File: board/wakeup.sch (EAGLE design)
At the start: 23 parts, among them IC2 ATMEGA48/88/168-AU, K1 PIN20X2, U1 EEPROM24

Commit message: Added pin header for tm1637 7-Segment display
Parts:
- added SL3: (no value), con-amp-quick:M04
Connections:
- net +5V: now also SL3.1
- net GND: now also SL3.4
- net MISO_SPI: now also SL3.2
- net SCLK_SPI: now also SL3.3
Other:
- note added: "CREE HiPower LED"
- note added: "Connector for TM1637 7-Segment Display"
- note added: "External Power Connector 5V"
- note added: "RaspberryPI GPIO Header"
- moved on the sheet: J1
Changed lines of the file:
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@@
 <part name="GND16" library="supply1" deviceset="GND" device=""/>
 <part name="P+3" library="supply1" deviceset="+5V" device=""/>
+<part name="SL3" library="con-amp-quick" deviceset="M04" device=""/>
+<part name="P+5" library="supply1" deviceset="+5V" device=""/>
+<part name="GND17" library="supply1" deviceset="GND" device=""/>
 </parts>
 <sheets>
@@
 <text x="289.56" y="16.51" size="1.778" layer="94" ratio="15">Checked  by:</text>
 <text x="374.65" y="5.08" size="2.54" layer="94" ratio="10">v0.1</text>
+<text x="127" y="165.1" size="1.778" layer="91">Connector for TM1637 7-Segment Display</text>
+<text x="40.64" y="111.76" size="1.778" layer="91">RaspberryPI GPIO Header</text>
+<text x="276.86" y="193.04" size="1.778" layer="91">CREE HiPower LED</text>
+<text x="198.12" y="231.14" size="1.778" layer="91">External Power Connector 5V</text>
 </plain>
 <instances>
@@
 <instance part="P+4" gate="VCC" x="134.62" y="127"/>
 <instance part="GND15" gate="1" x="134.62" y="78.74"/>
-<instance part="J1" gate="G$1" x="248.92" y="236.22"/>
+<instance part="J1" gate="G$1" x="205.74" y="238.76"/>
 <instance part="CREE_LED1" gate="G$1" x="320.04" y="238.76" rot="R90"/>
 <instance part="CREE_LED1" gate="G$2" x="320.04" y="200.66" rot="R90"/>
@@
 <attribute name="VALUE" x="203.2" y="210.82" size="1.778" layer="96" rot="R180"/>
 </instance>
+<instance part="SL3" gate="G$1" x="157.48" y="180.34" rot="R180"/>
+<instance part="P+5" gate="1" x="139.7" y="187.96" smashed="yes">
+<attribute name="VALUE" x="142.24" y="190.5" size="1.778" layer="96" rot="R180"/>
+</instance>
+<instance part="GND17" gate="1" x="139.7" y="172.72"/>
 </instances>
 <busses>
@@
 <pinref part="J1" gate="G$1" pin="2"/>
 <pinref part="J1" gate="G$1" pin="1"/>
-<wire x1="259.08" y1="236.22" x2="254" y2="236.22" width="0.1524" layer="91"/>
-<wire x1="254" y1="236.22" x2="254" y2="233.68" width="0.1524" layer="91"/>
-<label x="259.08" y="236.22" size="1.778" layer="95"/>
-<junction x="259.08" y="236.22"/>
-<junction x="254" y="236.22"/>
+<wire x1="215.9" y1="238.76" x2="210.82" y2="238.76" width="0.1524" layer="91"/>
+<wire x1="210.82" y1="238.76" x2="210.82" y2="236.22" width="0.1524" layer="91"/>
+<label x="215.9" y="238.76" size="1.778" layer="95"/>
+<junction x="215.9" y="238.76"/>
+<junction x="210.82" y="238.76"/>
 </segment>
 <segment>
@@
 <junction x="342.9" y="213.36"/>
 </segment>
+<segment>
+<pinref part="SL3" gate="G$1" pin="4"/>
+<wire x1="152.4" y1="175.26" x2="139.7" y2="175.26" width="0.1524" layer="91"/>
+<pinref part="GND17" gate="1" pin="GND"/>
+</segment>
 </net>
 <net name="+3V3" class="0">
@@
 <segment>
 <pinref part="J1" gate="G$1" pin="3"/>
-<wire x1="254" y1="238.76" x2="264.16" y2="238.76" width="0.1524" layer="91"/>
-<label x="264.16" y="238.76" size="1.778" layer="95"/>
-<junction x="264.16" y="238.76"/>
+<wire x1="210.82" y1="241.3" x2="220.98" y2="241.3" width="0.1524" layer="91"/>
+<label x="220.98" y="241.3" size="1.778" layer="95"/>
+<junction x="220.98" y="241.3"/>
+</segment>
+<segment>
+<pinref part="SL3" gate="G$1" pin="1"/>
+<wire x1="152.4" y1="182.88" x2="139.7" y2="182.88" width="0.1524" layer="91"/>
+<wire x1="139.7" y1="182.88" x2="139.7" y2="185.42" width="0.1524" layer="91"/>
+<pinref part="P+5" gate="1" pin="+5V"/>
 </segment>
 </net>
@@
 <label x="12.7" y="149.86" size="1.778" layer="95"/>
 </segment>
+<segment>
+<pinref part="SL3" gate="G$1" pin="2"/>
+<wire x1="152.4" y1="180.34" x2="139.7" y2="180.34" width="0.1524" layer="91"/>
+<label x="127" y="180.34" size="1.778" layer="95"/>
+</segment>
 </net>
 <net name="SCLK_SPI" class="0">
@@
 <label x="12.7" y="147.32" size="1.778" layer="95"/>
 </segment>
-</net>
+<segment>
+<pinref part="SL3" gate="G$1" pin="3"/>
+<wire x1="152.4" y1="177.8" x2="139.7" y2="177.8" width="0.1524" layer="91"/>
+<label x="127" y="177.8" size="1.778" layer="95"/>
+</segment>
+</net>

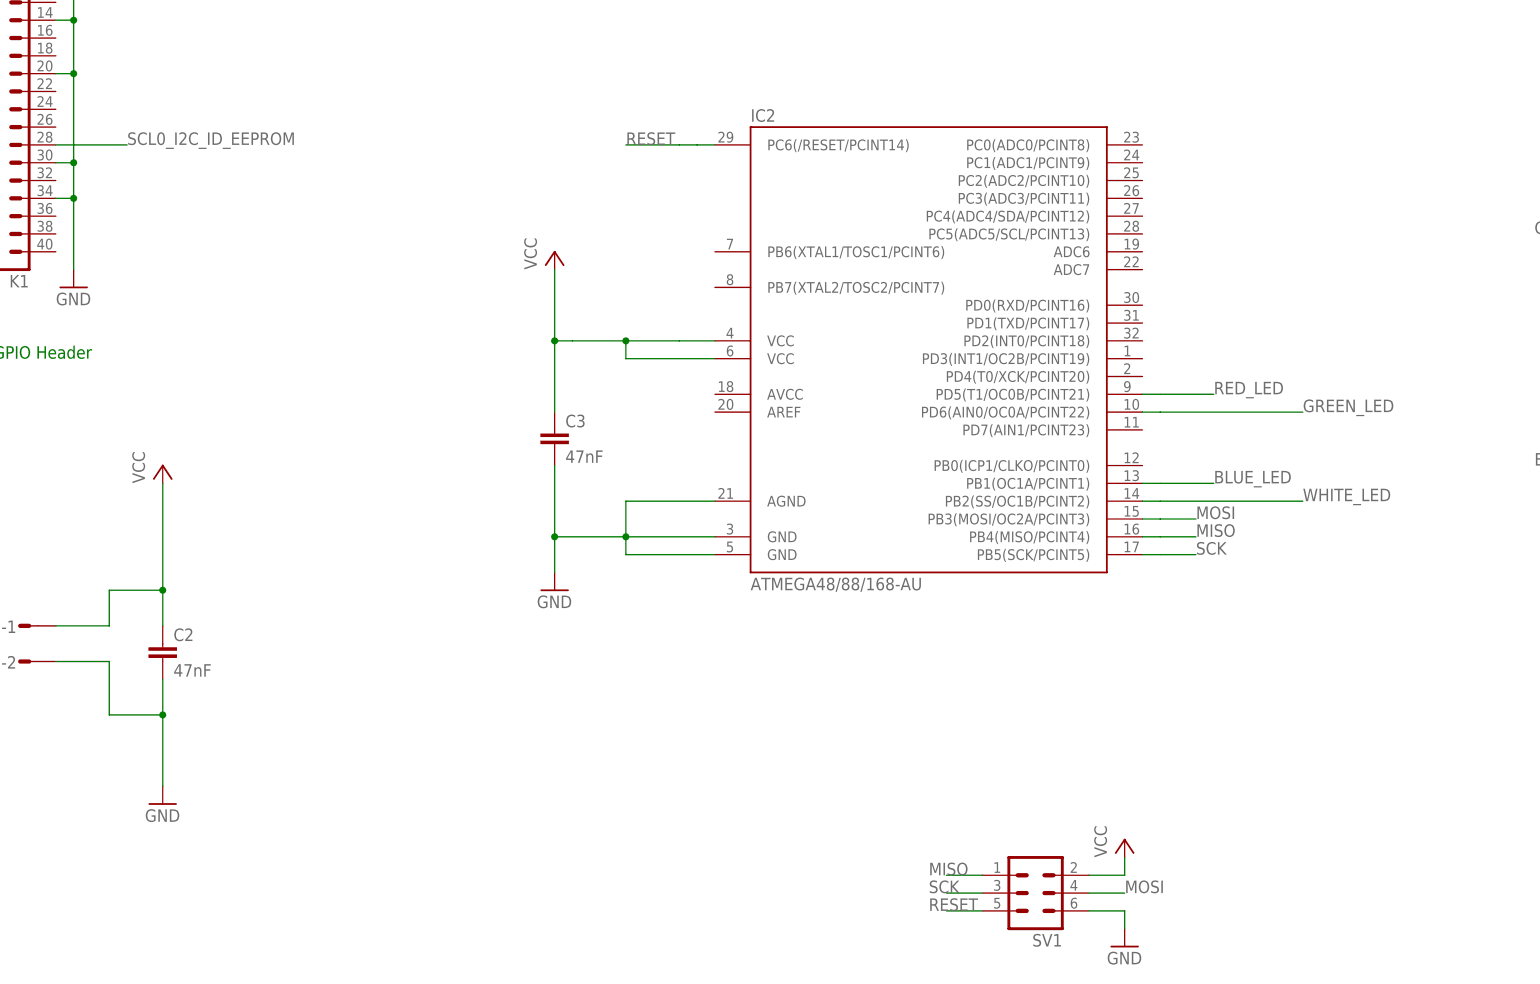
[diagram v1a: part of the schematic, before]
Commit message: Fixed FCC net, added I2C nets
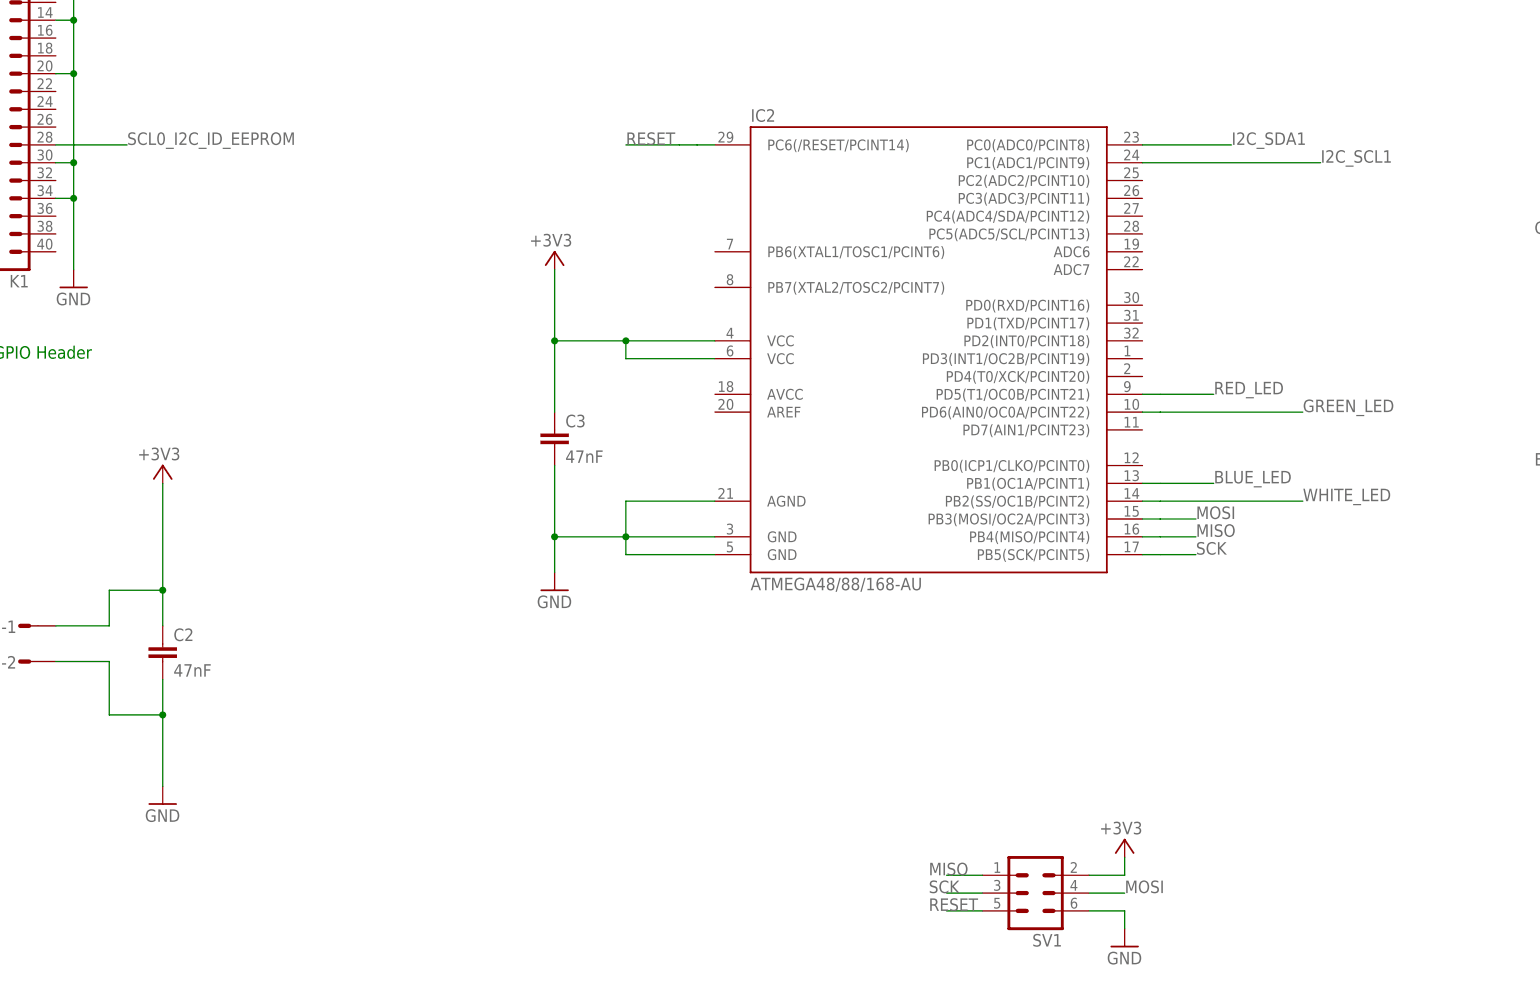
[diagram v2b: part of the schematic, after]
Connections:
- removed net VCC: C2.1, C3.1, IC2.VCC@1, IC2.VCC@2, SL2-1.S, SV1.2
- net +3V3: now also C2.1, C3.1, IC2.VCC@1, IC2.VCC@2, SL2-1.S, SV1.2
- net I2C_SCL1: now also IC2.PC1(ADC1/PCINT9)
- net I2C_SDA1: now also IC2.PC0(ADC0/PCINT8)
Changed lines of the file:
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@@
 <part name="P+1" library="supply1" deviceset="+5V" device=""/>
 <part name="SV1" library="con-ml" deviceset="ML6" device=""/>
-<part name="P+2" library="supply1" deviceset="VCC" device=""/>
 <part name="SL1" library="con-amp-quick" deviceset="M08" device=""/>
 <part name="GND6" library="supply1" deviceset="GND" device=""/>
 <part name="SL2" library="con-amp-quick" deviceset="M02S" device=""/>
 <part name="C2" library="rcl" deviceset="C-EU" device="C0805" value="47nF"/>
-<part name="P+7" library="supply1" deviceset="VCC" device=""/>
 <part name="GND7" library="supply1" deviceset="GND" device=""/>
 <part name="GND4" library="supply1" deviceset="GND" device=""/>
@@
 <part name="IC2" library="atmega8" deviceset="ATMEGA48/88/168" device="-AU"/>
 <part name="C3" library="rcl" deviceset="C-EU" device="C0805" value="47nF"/>
-<part name="P+4" library="supply1" deviceset="VCC" device=""/>
 <part name="GND15" library="supply1" deviceset="GND" device=""/>
 <part name="J1" library="con-jack" deviceset="JACK-PLUG" device="1"/>
@@
 <part name="P+5" library="supply1" deviceset="+5V" device=""/>
 <part name="GND17" library="supply1" deviceset="GND" device=""/>
+<part name="+3V2" library="supply1" deviceset="+3V3" device=""/>
+<part name="+3V3" library="supply1" deviceset="+3V3" device=""/>
+<part name="+3V6" library="supply1" deviceset="+3V3" device=""/>
 </parts>
 <sheets>
@@
 </instance>
 <instance part="SV1" gate="1" x="203.2" y="35.56" rot="R180"/>
-<instance part="P+2" gate="VCC" x="215.9" y="43.18"/>
 <instance part="SL1" gate="G$1" x="236.22" y="193.04" rot="R180"/>
 <instance part="GND6" gate="1" x="215.9" y="27.94"/>
@@
 <instance part="SL2" gate="-2" x="58.42" y="68.58"/>
 <instance part="C2" gate="G$1" x="78.74" y="71.12"/>
-<instance part="P+7" gate="VCC" x="78.74" y="96.52"/>
 <instance part="GND7" gate="1" x="78.74" y="48.26"/>
 <instance part="GND4" gate="1" x="302.26" y="152.4"/>
@@
 <instance part="IC2" gate="1" x="187.96" y="114.3"/>
 <instance part="C3" gate="G$1" x="134.62" y="101.6"/>
-<instance part="P+4" gate="VCC" x="134.62" y="127"/>
 <instance part="GND15" gate="1" x="134.62" y="78.74"/>
 <instance part="J1" gate="G$1" x="205.74" y="238.76"/>
@@
 </instance>
 <instance part="GND17" gate="1" x="139.7" y="172.72"/>
+<instance part="+3V2" gate="G$1" x="134.62" y="127" smashed="yes">
+<attribute name="VALUE" x="137.16" y="129.54" size="1.778" layer="96" rot="R180"/>
+</instance>
+<instance part="+3V3" gate="G$1" x="78.74" y="96.52" smashed="yes">
+<attribute name="VALUE" x="81.28" y="99.06" size="1.778" layer="96" rot="R180"/>
+</instance>
+<instance part="+3V6" gate="G$1" x="215.9" y="43.18" smashed="yes">
+<attribute name="VALUE" x="218.44" y="45.72" size="1.778" layer="96" rot="R180"/>
+</instance>
 </instances>
 <busses>
@@
 <junction x="43.18" y="175.26"/>
 </segment>
+<segment>
+<wire x1="157.48" y1="114.3" x2="144.78" y2="114.3" width="0.1524" layer="91"/>
+<wire x1="144.78" y1="114.3" x2="134.62" y2="114.3" width="0.1524" layer="91"/>
+<wire x1="134.62" y1="114.3" x2="134.62" y2="124.46" width="0.1524" layer="91"/>
+<pinref part="C3" gate="G$1" pin="1"/>
+<wire x1="134.62" y1="104.14" x2="134.62" y2="114.3" width="0.1524" layer="91"/>
+<junction x="134.62" y="114.3"/>
+<pinref part="IC2" gate="1" pin="VCC@2"/>
+<wire x1="157.48" y1="111.76" x2="144.78" y2="111.76" width="0.1524" layer="91"/>
+<wire x1="144.78" y1="111.76" x2="144.78" y2="114.3" width="0.1524" layer="91"/>
+<junction x="144.78" y="114.3"/>
+<pinref part="IC2" gate="1" pin="VCC@1"/>
+<pinref part="+3V2" gate="G$1" pin="+3V3"/>
+</segment>
+<segment>
+<wire x1="78.74" y1="78.74" x2="78.74" y2="93.98" width="0.1524" layer="91"/>
+<pinref part="C2" gate="G$1" pin="1"/>
+<wire x1="78.74" y1="73.66" x2="78.74" y2="78.74" width="0.1524" layer="91"/>
+<pinref part="SL2" gate="-1" pin="S"/>
+<wire x1="63.5" y1="73.66" x2="71.12" y2="73.66" width="0.1524" layer="91"/>
+<wire x1="71.12" y1="73.66" x2="71.12" y2="78.74" width="0.1524" layer="91"/>
+<wire x1="71.12" y1="78.74" x2="78.74" y2="78.74" width="0.1524" layer="91"/>
+<junction x="78.74" y="78.74"/>
+<pinref part="+3V3" gate="G$1" pin="+3V3"/>
+</segment>
+<segment>
+<pinref part="SV1" gate="1" pin="2"/>
+<wire x1="210.82" y1="38.1" x2="215.9" y2="38.1" width="0.1524" layer="91"/>
+<wire x1="215.9" y1="38.1" x2="215.9" y2="40.64" width="0.1524" layer="91"/>
+<pinref part="+3V6" gate="G$1" pin="+3V3"/>
+</segment>
 </net>
 <net name="SDA0_I2C_ID_EEPROM" class="0">
@@
 </segment>
 </net>
-<net name="VCC" class="0">
-<segment>
-<pinref part="P+7" gate="VCC" pin="VCC"/>
-<wire x1="78.74" y1="78.74" x2="78.74" y2="93.98" width="0.1524" layer="91"/>
-<pinref part="C2" gate="G$1" pin="1"/>
-<wire x1="78.74" y1="73.66" x2="78.74" y2="78.74" width="0.1524" layer="91"/>
-<pinref part="SL2" gate="-1" pin="S"/>
-<wire x1="63.5" y1="73.66" x2="71.12" y2="73.66" width="0.1524" layer="91"/>
-<wire x1="71.12" y1="73.66" x2="71.12" y2="78.74" width="0.1524" layer="91"/>
-<wire x1="71.12" y1="78.74" x2="78.74" y2="78.74" width="0.1524" layer="91"/>
-<junction x="78.74" y="78.74"/>
-</segment>
-<segment>
-<pinref part="SV1" gate="1" pin="2"/>
-<pinref part="P+2" gate="VCC" pin="VCC"/>
-<wire x1="210.82" y1="38.1" x2="215.9" y2="38.1" width="0.1524" layer="91"/>
-<wire x1="215.9" y1="38.1" x2="215.9" y2="40.64" width="0.1524" layer="91"/>
-</segment>
-<segment>
-<pinref part="P+4" gate="VCC" pin="VCC"/>
-<wire x1="152.4" y1="114.3" x2="144.78" y2="114.3" width="0.1524" layer="91"/>
-<wire x1="144.78" y1="114.3" x2="137.16" y2="114.3" width="0.1524" layer="91"/>
-<wire x1="137.16" y1="114.3" x2="134.62" y2="114.3" width="0.1524" layer="91"/>
-<wire x1="134.62" y1="114.3" x2="134.62" y2="124.46" width="0.1524" layer="91"/>
-<pinref part="C3" gate="G$1" pin="1"/>
-<wire x1="134.62" y1="104.14" x2="134.62" y2="114.3" width="0.1524" layer="91"/>
-<junction x="134.62" y="114.3"/>
-<pinref part="IC2" gate="1" pin="VCC@2"/>
-<wire x1="157.48" y1="111.76" x2="144.78" y2="111.76" width="0.1524" layer="91"/>
-<wire x1="144.78" y1="111.76" x2="144.78" y2="114.3" width="0.1524" layer="91"/>
-<junction x="144.78" y="114.3"/>
-<pinref part="IC2" gate="1" pin="VCC@1"/>
-<wire x1="157.48" y1="114.3" x2="152.4" y2="114.3" width="0.1524" layer="91"/>
-</segment>
-</net>
 <net name="MOSI" class="0">
 <segment>
@@
 <label x="27.94" y="172.72" size="1.778" layer="95"/>
 </segment>
+<segment>
+<pinref part="IC2" gate="1" pin="PC0(ADC0/PCINT8)"/>
+<wire x1="218.44" y1="142.24" x2="231.14" y2="142.24" width="0.1524" layer="91"/>
+<label x="231.14" y="142.24" size="1.778" layer="95"/>
+</segment>
 </net>
 <net name="I2C_SCL1" class="0">
@@
 <label x="27.94" y="170.18" size="1.778" layer="95"/>
 </segment>
-</net>
+<segment>
+<pinref part="IC2" gate="1" pin="PC1(ADC1/PCINT9)"/>
+<wire x1="218.44" y1="139.7" x2="243.84" y2="139.7" width="0.1524" layer="91"/>
+<label x="243.84" y="139.7" size="1.778" layer="95"/>
+</segment>
+</net>

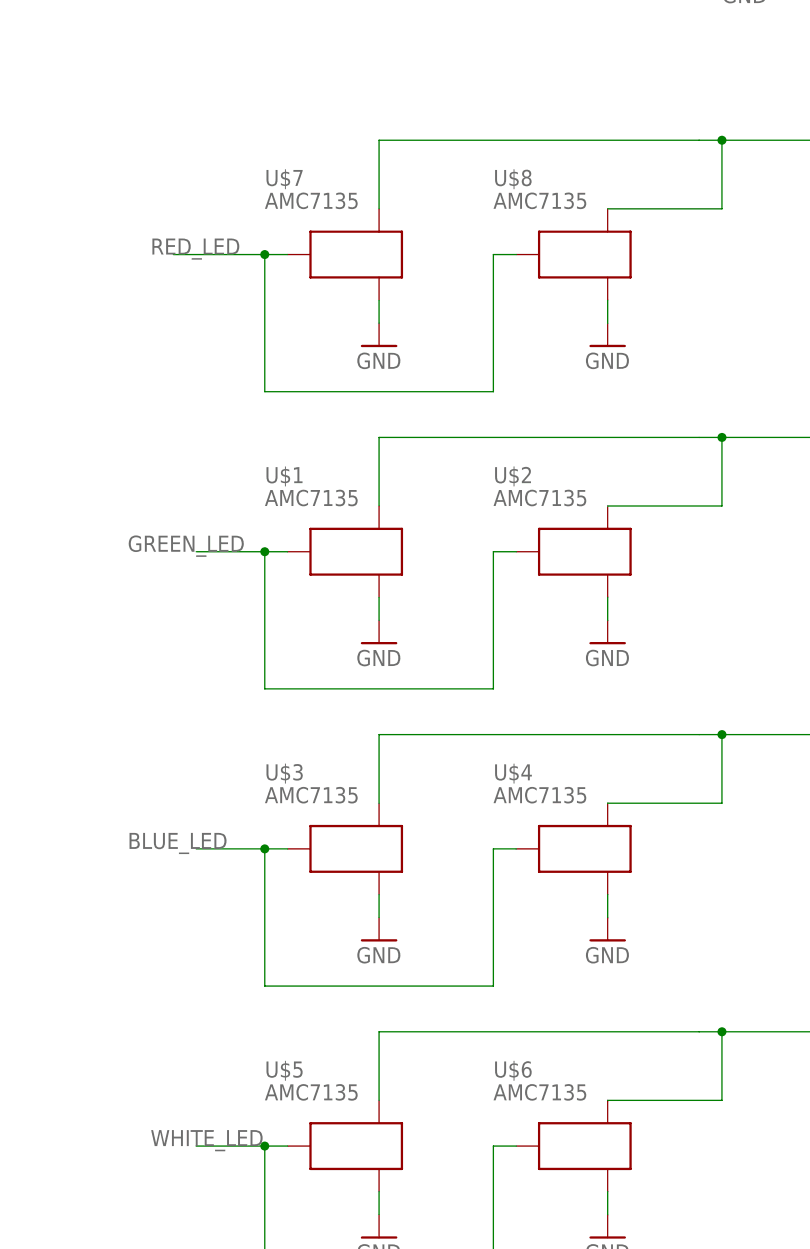
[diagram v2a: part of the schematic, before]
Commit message: Fixed some naming and added tag
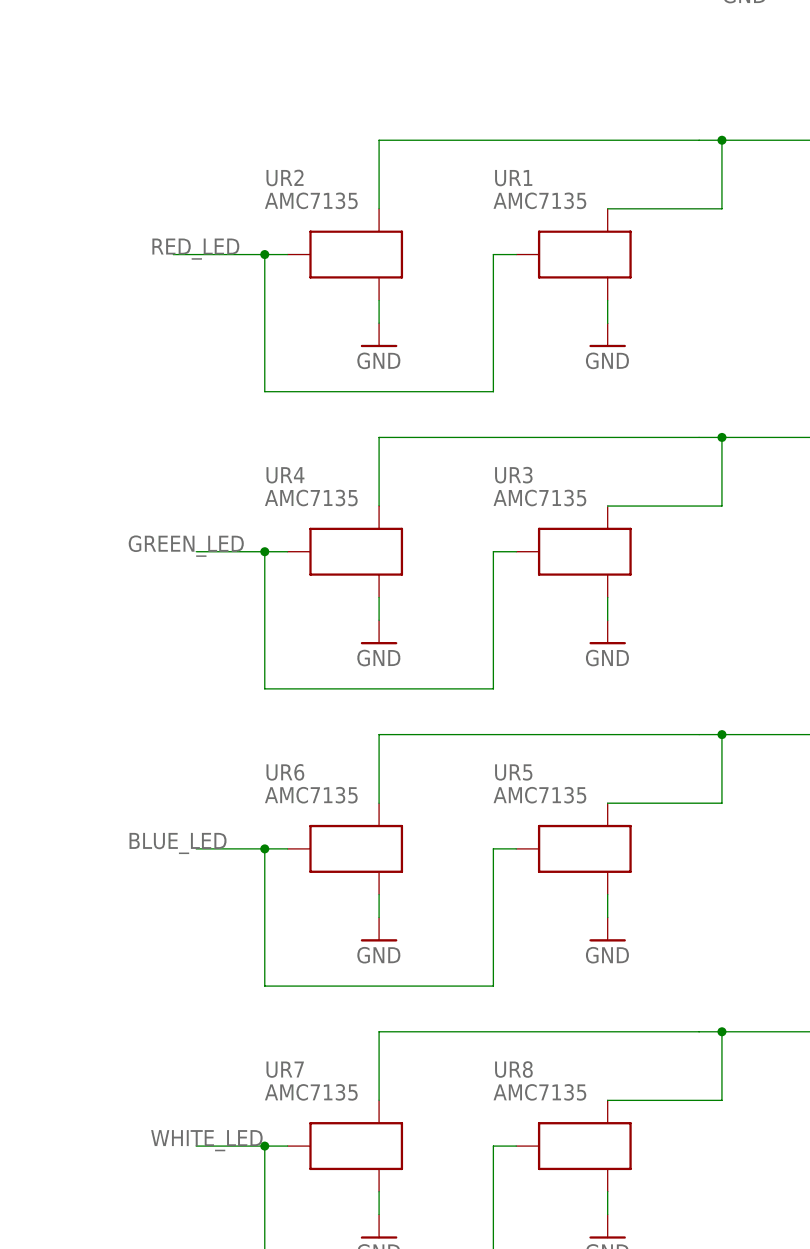
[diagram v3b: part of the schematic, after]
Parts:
- renumbered U$1 to UR4, U$2 to UR3, U$3 to UR6, U$4 to UR5, U$5 to UR7, U$6 to UR8, U$7 to UR2, U$8 to UR1
